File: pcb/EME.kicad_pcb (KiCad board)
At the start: 2 copper layers, 42 parts, among them J1 BMP180, J10 INPUT ONLY, J11 UART0, J12 SPI_CONN, J13 UART0, J2 ReedSwitchX8, J3 SS41, J5 PanelSolar, J6 BH1750, J7 DHT22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

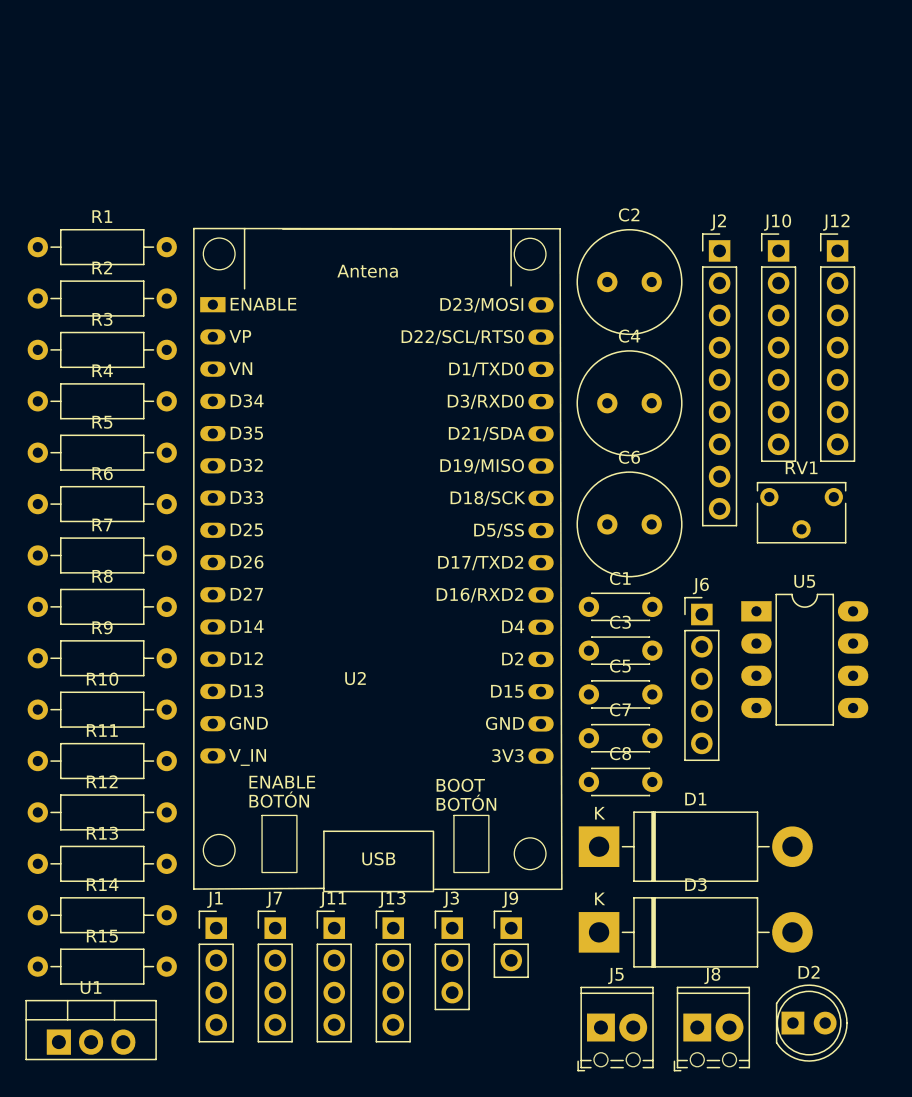
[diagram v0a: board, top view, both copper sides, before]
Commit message: se agregaron ejemplos de los sensores y actualizo la PCB
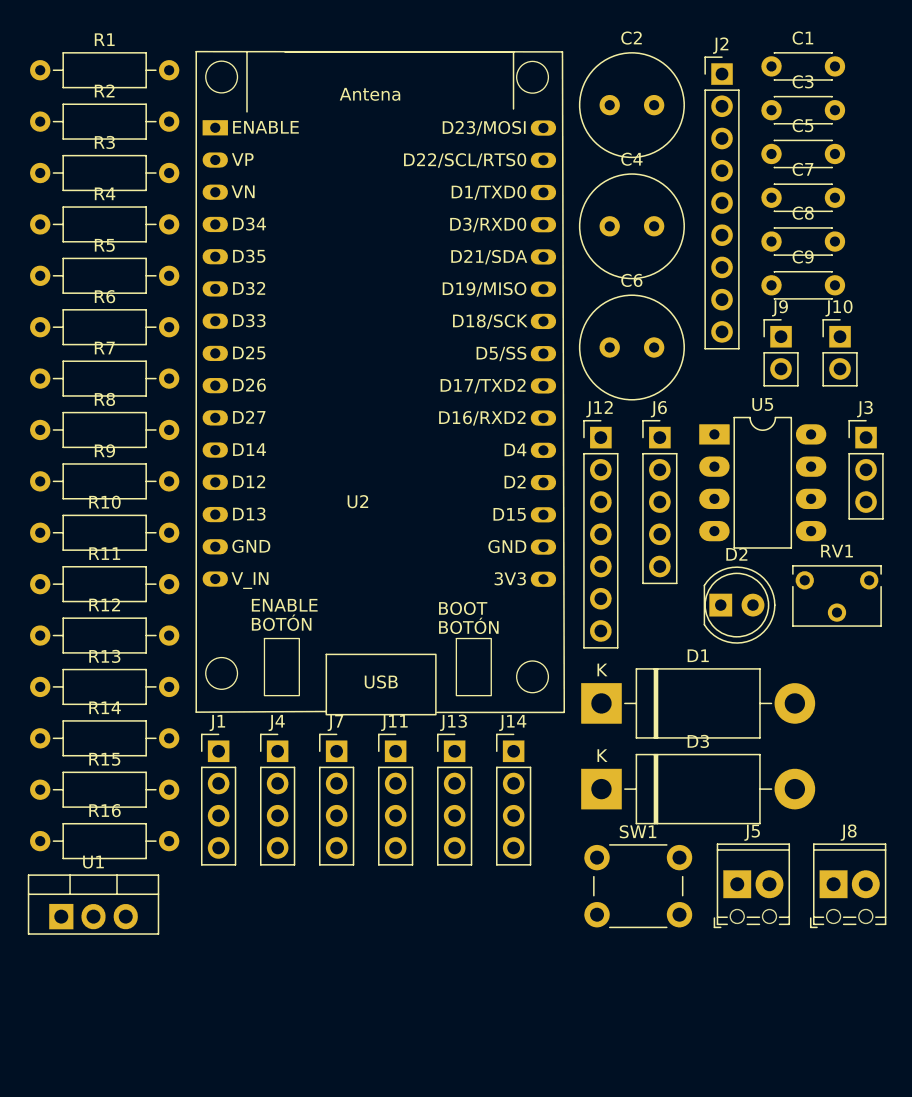
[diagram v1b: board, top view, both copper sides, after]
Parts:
- added C9: 104, Capacitor_THT:C_Disc_D4.3mm_W1.9mm_P5.00mm, F.Cu at (156.4, 68.1)
- added J14: MQ135, Connector_PinHeader_2.54mm:PinHeader_1x04_P2.54mm_Vertical, F.Cu at (136.1, 104.8)
- added J4: Hoja Mojada, Connector_PinHeader_2.54mm:PinHeader_1x04_P2.54mm_Vertical, F.Cu at (117.5, 104.8)
- added R16: 10k, Resistor_THT:R_Axial_DIN0207_L6.3mm_D2.5mm_P10.16mm_Horizontal, F.Cu at (98.7, 111.9)
- added SW1: Enable, Button_Switch_THT:SW_PUSH_6mm_H8mm, F.Cu at (142.6, 113.2)
- J10: value INPUT ONLY -> Reset; footprint Connector_PinHeader_2.54mm:PinHeader_1x07_P2.54mm_Vertical -> Connector_PinHeader_2.54mm:PinHeader_1x02_P2.54mm_Vertical
- J13: value UART0 -> UART2
- moved J9 51.2 mm to (157.1, 72.1)
- moved J3 50.6 mm to (163.8, 80.1)
- moved C3 45.0 mm to (156.4, 54.3)
- moved C5 45.0 mm to (156.4, 57.7)
- moved C1 45.0 mm to (156.4, 50.8)
- moved C7 45.0 mm to (156.4, 61.2)
- moved C8 45.0 mm to (156.4, 64.6)
- moved D2 33.4 mm to (152.4, 93.3)
- moved J12 23.8 mm to (142.9, 80.1)
- moved J5 15.6 mm to (153.7, 115.3)
- moved J8 15.6 mm to (161.3, 115.3)
- moved J11 14.8 mm to (126.8, 104.8)
- moved J13 14.8 mm to (131.4, 104.8)
- moved J7 14.8 mm to (122.1, 104.8)
- moved J6 14.3 mm to (147.6, 80.1)
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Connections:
- C8 pad 1: +5V -> +3.3V
- J10 pad 1: Net-(J10-Pin_1) -> GNDREF
- R5 pad 2: +5V -> +3.3V
- R6 pad 2: +5V -> +3.3V
- R7 pad 2: +5V -> +3.3V
- U2 pad 1: Net-(J10-Pin_5) -> Net-(J10-Pin_2)
- U2 pad 2: Net-(J10-Pin_4) -> KY-004_Dg
- U2 pad 3: Net-(J10-Pin_3) -> KY-004_An
- U2 pad 4: Net-(J10-Pin_2) -> MQ135_Dg
- U2 pad 5: Net-(J10-Pin_1) -> MQ135_An

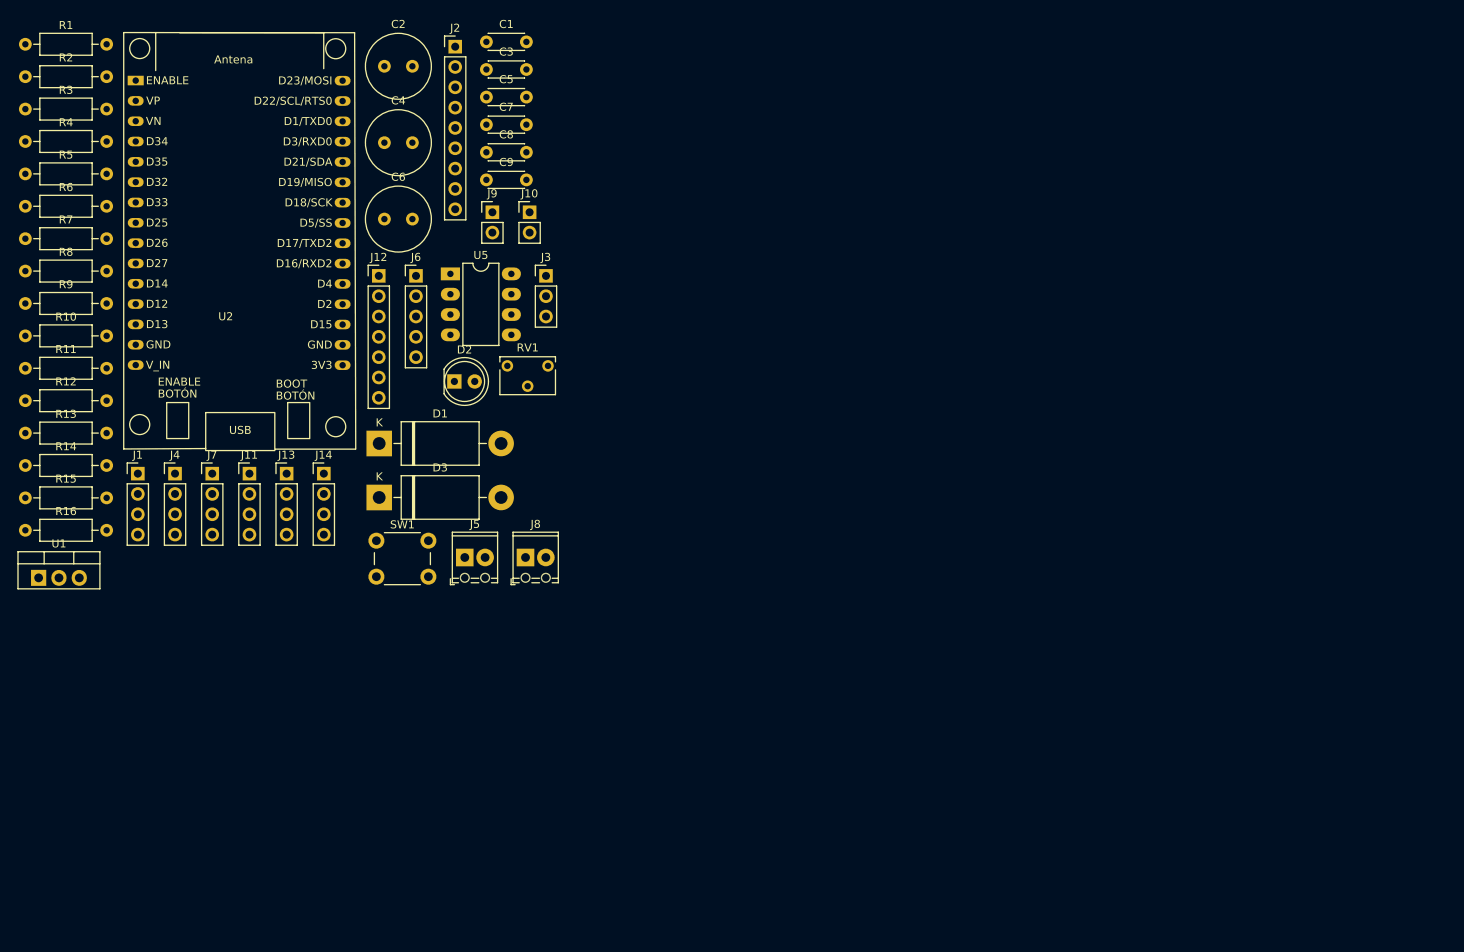
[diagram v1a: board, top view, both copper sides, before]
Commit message: Se armó diseño de PCB y se decoró esquemático
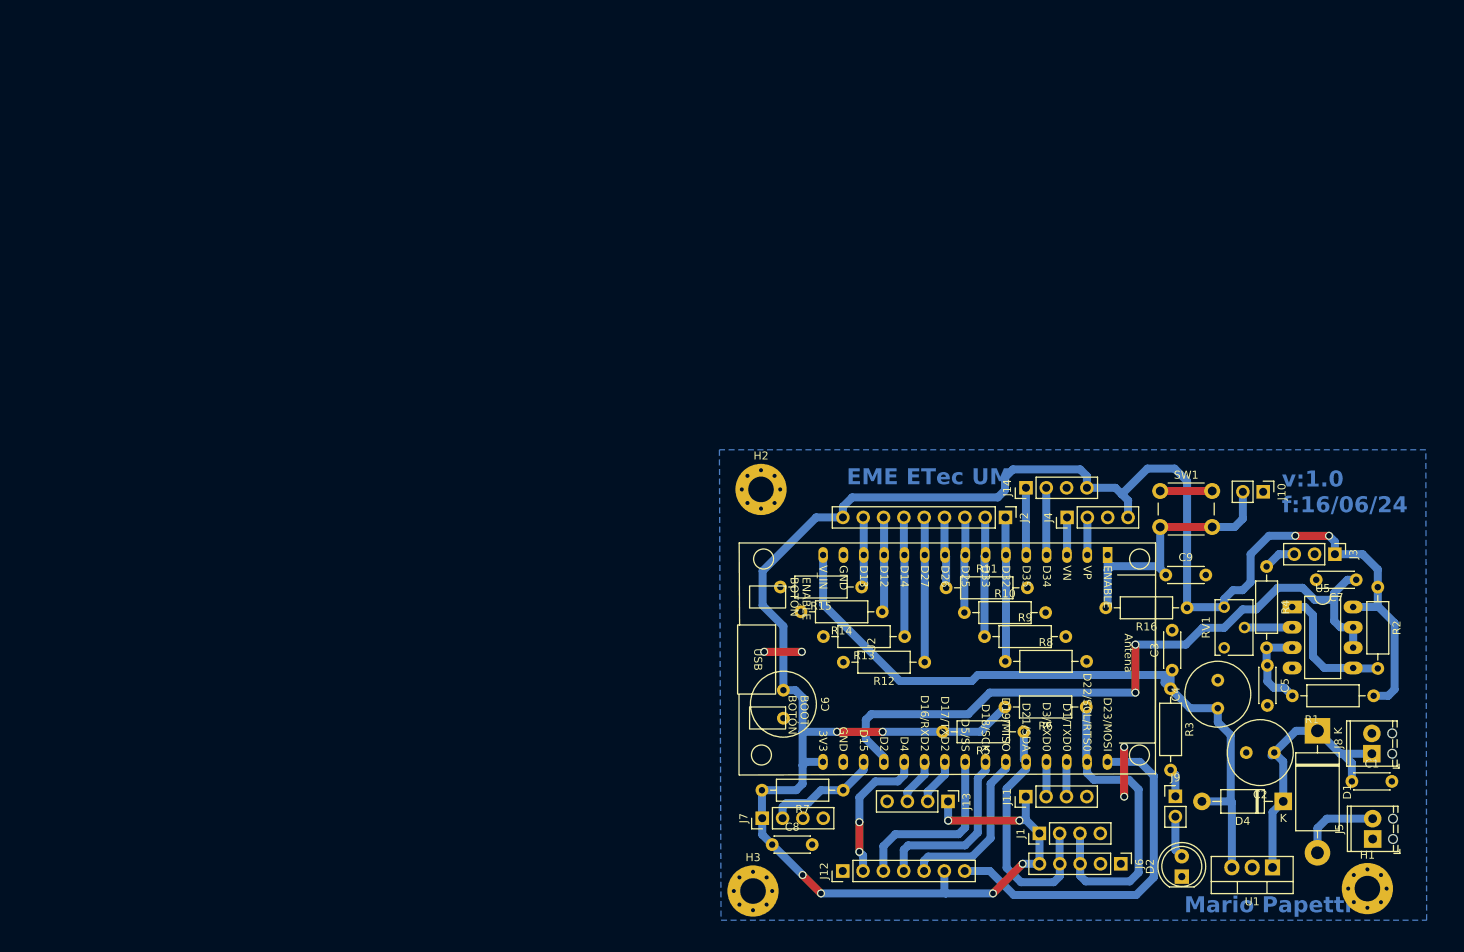
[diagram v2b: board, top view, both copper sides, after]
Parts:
- removed D3: 1N5400, Diode_THT:D_DO-201AD_P15.24mm_Horizontal
- added D4: 1N4007, Diode_THT:D_DO-41_SOD81_P10.16mm_Horizontal, F.Cu at (256.0, 145.8)
- added H1: Sujeción GND, MountingHole:MountingHole_3.2mm_M3_Pad_Via, F.Cu at (266.5, 156.7)
- added H2: Sujeción GND, MountingHole:MountingHole_3.2mm_M3_Pad_Via, F.Cu at (190.7, 106.8)
- added H3: Sujeción GND, MountingHole:MountingHole_3.2mm_M3_Pad_Via, F.Cu at (189.7, 157.0)
- moved R1 187.2 mm to (267.3, 132.6), turned to 180 degrees
- moved R2 180.7 mm to (267.8, 119.0), turned to -90 degrees
- moved R4 164.0 mm to (253.9, 116.4), turned to -90 degrees
- moved R3 160.4 mm to (241.9, 131.7), turned to -90 degrees
- moved U1 158.4 mm to (254.6, 154.0), turned to 180 degrees
- moved R6 146.6 mm to (231.4, 134.0), turned to 180 degrees
- moved R16 145.5 mm to (244.0, 121.6), turned to 180 degrees
- moved R5 143.0 mm to (223.6, 137.1), turned to 180 degrees
- moved C1 142.3 mm to (264.6, 143.3)
- moved C2 140.5 mm to (254.9, 139.7), turned to 180 degrees
- moved U2 135.2 mm to (234.0, 114.9), turned to -90 degrees
- moved R8 131.9 mm to (221.2, 128.3)
- moved R9 126.9 mm to (218.6, 125.2)
- moved C4 125.9 mm to (247.8, 134.1), turned to 90 degrees
- moved R7 123.3 mm to (201.0, 144.4), turned to 180 degrees
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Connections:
- J1 pad 3: SCL -> SDA
- J12 pad 6: Net-(J12-Pin_6) -> +3.3V
- J12 pad 7: +3.3V -> Net-(J12-Pin_7)
- J6 pad 1: +3.3V -> ADDR
- J6 pad 3: SCL -> SDA
- J6 pad 5: ADDR -> +3.3V
- R6 pad 1: SCL -> SDA
- U2 pad 29: SCL -> SDA
- U2 pad 30: Net-(J12-Pin_6) -> Net-(J12-Pin_7)
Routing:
- net +3.3V: track 0.00 -> 271.4 mm, vias 0 -> 10
- net +5V: track 0.00 -> 89.1 mm
- net D_hall: track 0.00 -> 87.9 mm, vias 0 -> 2
- net Net-(J12-Pin_7): track 0.00 -> 45.0 mm
- net SDA: track 0.00 -> 39.3 mm
- net +BATT: track 0.00 -> 34.3 mm
- net Net-(J10-Pin_2): track 0.00 -> 34.1 mm
- net SCL: track 0.00 -> 31.2 mm
- net Net-(J12-Pin_3): track 0.00 -> 22.5 mm
- net Net-(J12-Pin_4): track 0.00 -> 22.0 mm
- net Net-(J12-Pin_5): track 0.00 -> 21.1 mm
- net Net-(J2-Pin_5): track 0.00 -> 18.1 mm
- net Net-(J2-Pin_1): track 0.00 -> 18.1 mm
- net Net-(J12-Pin_2): track 0.00 -> 17.8 mm, vias 0 -> 2
- net GNDREF: track 0.00 -> 17.4 mm, vias 0 -> 4
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- added copper zone on B.Cu, net GNDREF
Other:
- board text added: "EME ETec UM"
- board text added: "Mario Papetti"
- board text added: "v:1.0 f:16/06/24"

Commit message: Add files via upload
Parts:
- removed J2: ReedSwitchX8, Connector_PinHeader_2.54mm:PinHeader_1x09_P2.54mm_Vertical
- removed R10, R11, R12, R13, R14, R15, R8, R9: 10k, Resistor_THT:R_Axial_DIN0207_L6.3mm_D2.5mm_P10.16mm_Horizontal
- added J15: AS5600, Connector_PinHeader_2.54mm:PinHeader_1x05_P2.54mm_Vertical, F.Cu at (219.7, 108.6)
- moved H2 1.47 mm to (189.2, 106.7)
- moved H3 0.48 mm to (189.2, 156.8)
- moved C1 0.26 mm to (264.6, 143.5)
- moved J7 0.10 mm to (190.9, 148.0)
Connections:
- J1 pad 2: SCL -> SDA
- J1 pad 3: SDA -> SCL
- J6 pad 3: SDA -> SCL
- J6 pad 4: SCL -> SDA
- R5 pad 1: SCL -> SDA
- R6 pad 1: SDA -> SCL
- U2 pad 10: Net-(J2-Pin_5) -> unconnected-(U2-D27/ADC2_7/T7/~-Pad10)
- U2 pad 11: Net-(J2-Pin_6) -> unconnected-(U2-D14/ADC2_6/HSPI_CLK/T6/~-Pad11)
- U2 pad 12: Net-(J2-Pin_7) -> unconnected-(U2-D12/ADC2_5/HSPI_Q/T5/~-Pad12)
- U2 pad 13: Net-(J2-Pin_8) -> unconnected-(U2-D13/ADC2_4/HSPI_ID/T4/~-Pad13)
- U2 pad 26: SCL -> SDA
- U2 pad 29: SDA -> SCL
- U2 pad 7: Net-(J2-Pin_2) -> unconnected-(U2-D33/ADC1_5/T8/~-Pad7)
- U2 pad 8: Net-(J2-Pin_3) -> unconnected-(U2-D25/ADC2_8/DAC1/~-Pad8)
- U2 pad 9: Net-(J2-Pin_4) -> unconnected-(U2-D26/ADC2_9/DAC2/~-Pad9)
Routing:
- net SCL: track 31.2 -> 112.4 mm, vias 0 -> 4
- net SDA: track 39.3 -> 98.5 mm, vias 0 -> 4
- net Net-(J2-Pin_5): track 18.1 -> 0.00 mm
- net Net-(J2-Pin_2): track 15.0 -> 0.00 mm
- net Net-(J2-Pin_6): track 14.9 -> 0.00 mm
- net Net-(J2-Pin_3): track 12.0 -> 0.00 mm
- net Net-(J2-Pin_7): track 11.9 -> 0.00 mm
- net Net-(J15-Pin_1): track 18.1 -> 6.40 mm
- net Net-(J2-Pin_8): track 8.93 -> 0.00 mm
- net Net-(J2-Pin_4): track 8.88 -> 0.00 mm
- net +3.3V: track 271.4 -> 276.4 mm
- net +5V: track 89.1 -> 86.0 mm
